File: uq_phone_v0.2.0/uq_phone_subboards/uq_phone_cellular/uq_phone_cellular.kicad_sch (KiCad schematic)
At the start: 28 parts, among them J1 513382474, J2 513382474, J3 20279-001E-03, J4 20279-001E-03, U1 WP SNAP-IN BASE_6000636

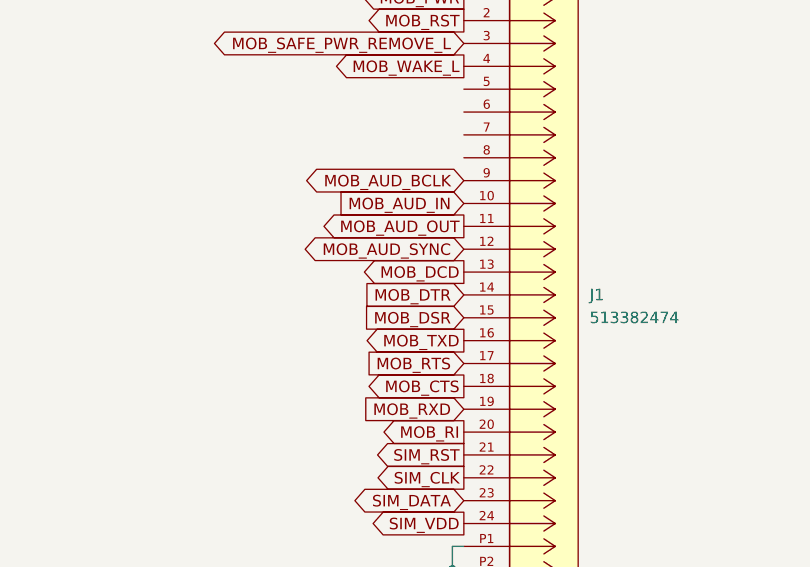
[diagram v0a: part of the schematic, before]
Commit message: New logic level shifters
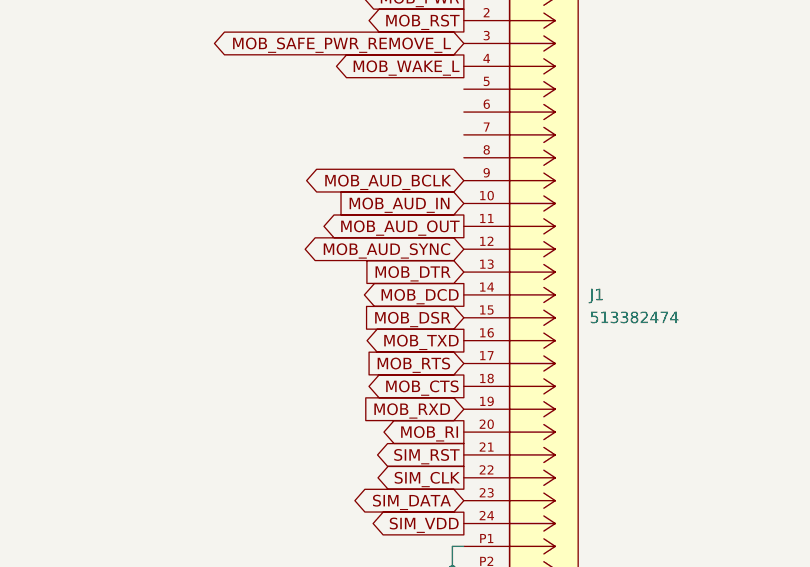
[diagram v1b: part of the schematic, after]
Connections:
- net MOB_DCD: now also J1.14; no longer J1.13
- net MOB_DTR: now also J1.13; no longer J1.14
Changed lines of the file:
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@@
-		)
-	)
-	(global_label "MOB_DCD"
-		(shape output)
-		(at 130.81 236.22 180)
-		(fields_autoplaced yes)
-		(effects
-			(font
-				(size 1.27 1.27)
-			)
-			(justify right)
-		)
-		(property "Intersheetrefs" "${INTERSHEET_REFS}"
-			(at 118.9953 236.22 0)
-			(effects
-				(font
-					(size 1.27 1.27)
-				)
-				(justify right)
-				(hide yes)
-			)
 		)
 	)
@@
 		)
 	)
-	(global_label "MOB_DTR"
-		(shape input)
+	(global_label "MOB_DCD"
+		(shape output)
 		(at 130.81 238.76 180)
 		(fields_autoplaced yes)
@@
 		)
 		(property "Intersheetrefs" "${INTERSHEET_REFS}"
-			(at 119.2977 238.76 0)
+			(at 118.9953 238.76 0)
 			(effects
 				(font
@@
 			(effects
 				(font
+					(size 1.27 1.27)
+				)
+				(justify right)
+				(hide yes)
+			)
+		)
+	)
+	(global_label "MOB_DTR"
+		(shape input)
+		(at 130.81 236.22 180)
+		(fields_autoplaced yes)
+		(effects
+			(font
+				(size 1.27 1.27)
+			)
+			(justify right)
+		)
+		(property "Intersheetrefs" "${INTERSHEET_REFS}"
+			(at 119.2977 236.22 0)
+			(effects
+				(font

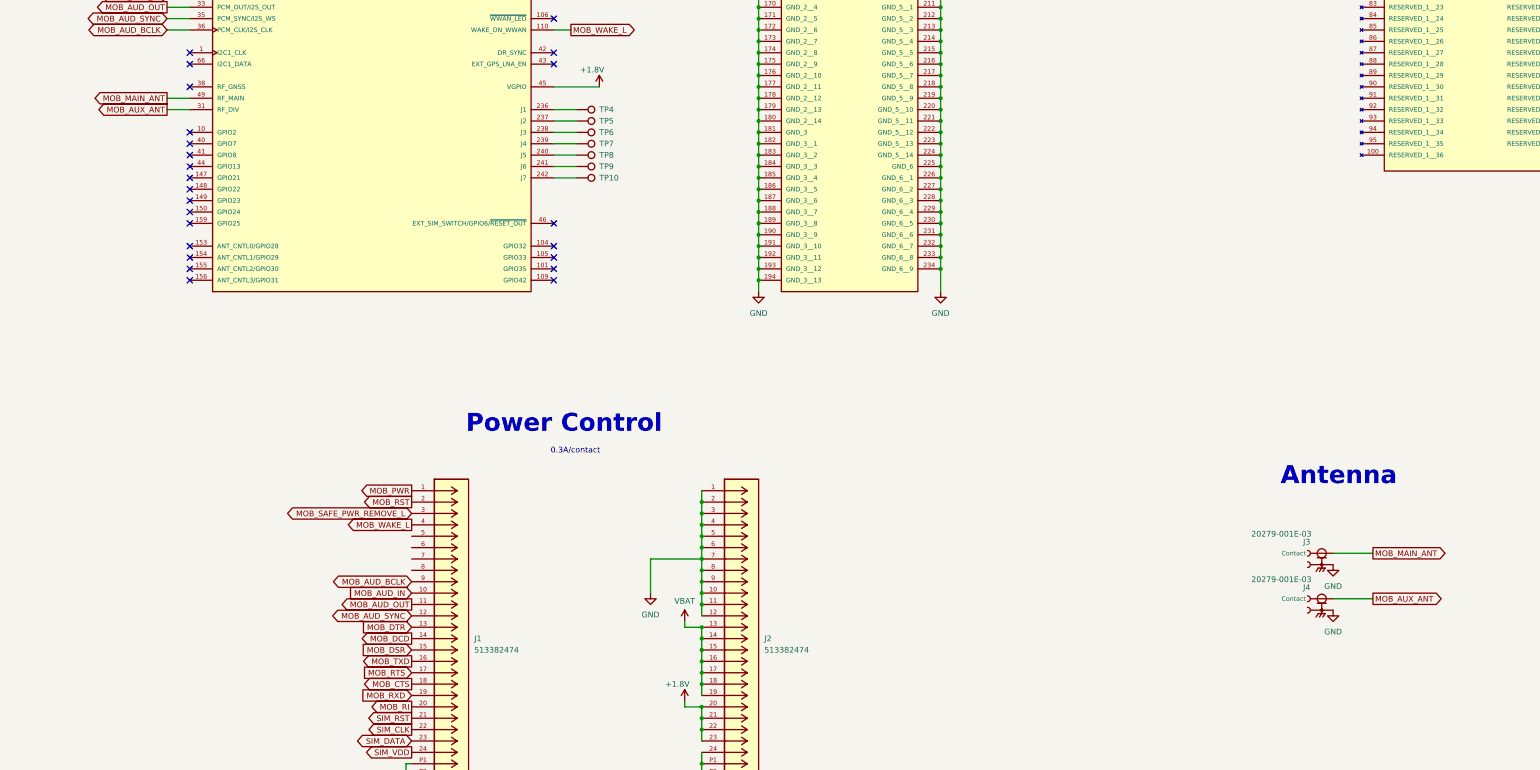
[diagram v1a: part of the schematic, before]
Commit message: Add GNSS antenna for sag
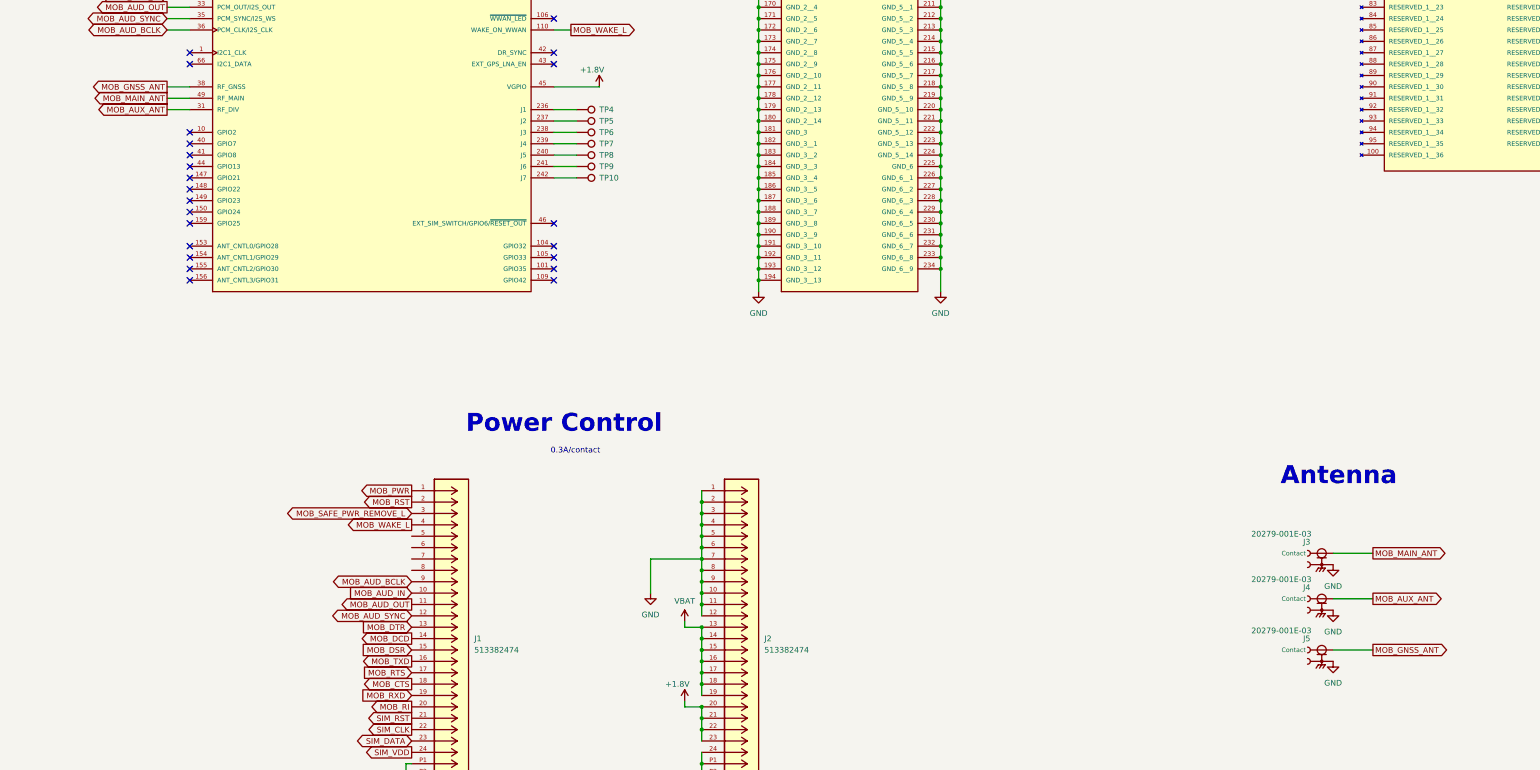
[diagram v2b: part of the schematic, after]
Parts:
- added J5: 20279-001E-03, 20279-001E-03:IPEX_20279-001E-03, symbol 20279-001E-03:20279-001E-03
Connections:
- net GND: now also J5.2
- net MOB_GNSS_ANT: now reaches U1.38 (RF_GNSS)
- net MOB_GNSS_ANT: now also J5.1 (Contact)
- no-connect marks 42 -> 41

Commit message: Cleaning up adn fixing massive mistake
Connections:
- net GND: now also J1.5, J1.6, J1.7, J1.8
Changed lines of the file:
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@@
 	)
 	(junction
+		(at 130.81 220.98)
+		(diameter 0)
+		(color 0 0 0 0)
+	)
+	(junction
 		(at 248.92 156.21)
 		(diameter 0)
@@
 	)
 	(junction
+		(at 130.81 218.44)
+		(diameter 0)
+		(color 0 0 0 0)
+	)
+	(junction
 		(at 208.28 54.61)
 		(diameter 0)
@@
 	)
 	(junction
+		(at 130.81 215.9)
+		(diameter 0)
+		(color 0 0 0 0)
+	)
+	(junction
 		(at 248.92 113.03)
 		(diameter 0)
@@
 	(wire
 		(pts
+			(xy 130.81 218.44) (xy 130.81 220.98)
+		)
+		(stroke
+			(width 0)
+			(type default)
+		)
+	)
+	(wire
+		(pts
 			(xy 130.81 271.78) (xy 129.54 271.78)
 		)
@@
 	(wire
 		(pts
+			(xy 124.46 215.9) (xy 130.81 215.9)
+		)
+		(stroke
+			(width 0)
+			(type default)
+		)
+	)
+	(wire
+		(pts
 			(xy 162.56 102.87) (xy 166.37 102.87)
 		)
@@
 	(wire
 		(pts
+			(xy 130.81 220.98) (xy 130.81 223.52)
+		)
+		(stroke
+			(width 0)
+			(type default)
+		)
+	)
+	(wire
+		(pts
 			(xy 312.42 52.07) (xy 304.8 52.07)
 		)
@@
 	(wire
 		(pts
+			(xy 124.46 218.44) (xy 124.46 215.9)
+		)
+		(stroke
+			(width 0)
+			(type default)
+		)
+	)
+	(wire
+		(pts
 			(xy 195.58 254) (xy 195.58 256.54)
 		)
@@
 	(wire
 		(pts
+			(xy 130.81 215.9) (xy 130.81 218.44)
+		)
+		(stroke
+			(width 0)
+			(type default)
+		)
+	)
+	(wire
+		(pts
 			(xy 195.58 256.54) (xy 195.58 259.08)
 		)
@@
 					(unit 1)
 				)
+			)
+		)
+	)
+	(symbol
+		(lib_id "power:GND")
+		(at 124.46 218.44 0)
+		(unit 1)
+		(exclude_from_sim no)
+		(in_bom yes)
+		(on_board yes)
+		(dnp no)
+		(property "Reference" "#PWR014"
+			(at 124.46 224.79 0)
+			(effects
+				(font
+					(size 1.27 1.27)
+				)
+				(hide yes)
+			)
+		)
+		(property "Value" "GND"
+			(at 124.46 223.266 0)
+			(effects
+				(font
+					(size 1.27 1.27)
+				)
+			)
+		)
+		(property "Footprint" ""
+			(at 124.46 218.44 0)
+			(effects
+				(font
+					(size 1.27 1.27)
+				)
+				(hide yes)
+			)
+		)
+		(property "Datasheet" ""
+			(at 124.46 218.44 0)
+			(effects
+				(font
+					(size 1.27 1.27)
+				)
+				(hide yes)
+			)
+		)
+		(property "Description" "Power symbol creates a global label with name \"GND\" , ground"
+			(at 124.46 218.44 0)
+			(effects
+				(font
+					(size 1.27 1.27)
+				)
+				(hide yes)
+			)
+		)
+		(pin "1"
+		)
+		(instances
+			(project "uq_phone_cellular"
+				(path "/ec1b925e-10f6-47b3-b240-fe8bcf33326b"
+					(reference "#PWR014")
+					(unit 1)
+				)
